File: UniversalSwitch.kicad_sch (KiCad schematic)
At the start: 30 parts, among them IC1501 TPS259830ONRGER, IC1502 TPS259830ONRGER, Q1501 NVTFWS4D9N04XMTAG, Q1502 NVTFWS4D9N04XMTAG

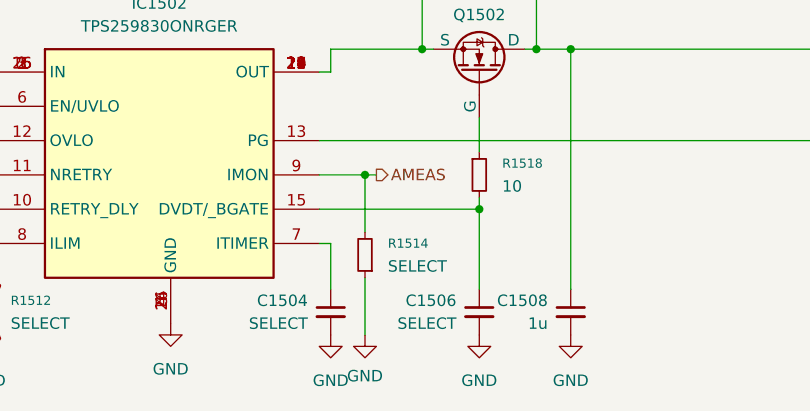
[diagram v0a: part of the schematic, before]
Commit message: Minor changes to acomodate jlcpcb guidelines, this version ordered
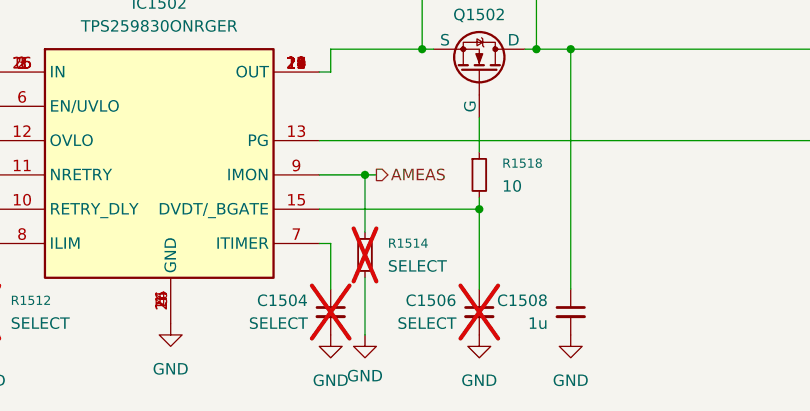
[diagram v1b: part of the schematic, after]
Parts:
- C1504, C1506, R1514: now not fitted

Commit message: nearly finnished CORE pcb
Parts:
- renumbered C1501 to C4502, C1502 to C4504, C1503 to C4506, C1504 to C4508, C1505 to C4509, C1506 to C4510, C1507 to C4511, C1508 to C4512, IC1501 to IC4501, IC1502 to IC4502, Q1501 to Q4501, Q1502 to Q4502, R1501 to R4502, R1502 to R4503, R1503 to R4504, R1504 to R4505, R1505 to R4506, R1506 to R4508, R1507 to R4509, R1508 to R4510, R1509 to R4511, R1510 to R4512, R1511 to R4513, R1512 to R4514, R1513 to R4515, R1514 to R4516, R1515 to R4517, R1516 to R4518, R1517 to R4519, R1518 to R4520

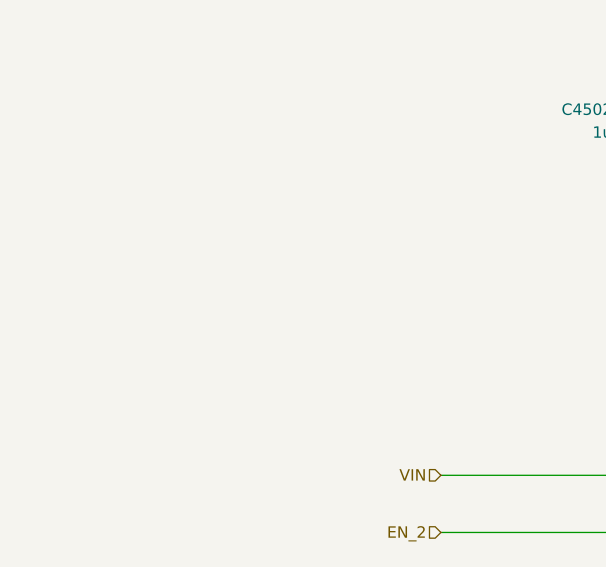
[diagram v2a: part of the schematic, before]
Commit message: pcb progres for all components
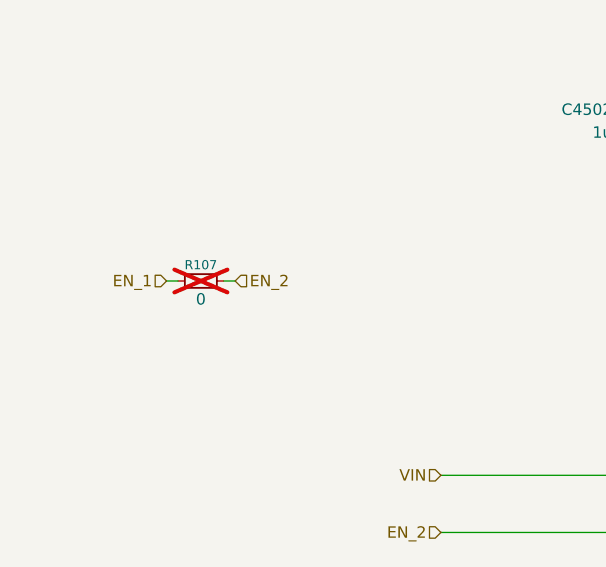
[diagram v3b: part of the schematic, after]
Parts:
- added R107: 0, Resistor_SMD:R_0603_1608Metric_Pad0.98x0.95mm_HandSolder, symbol Device:R_Small
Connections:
- net EN_1: now also R107.1
- net EN_2: now also R107.2

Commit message: progress on PCBs
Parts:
- removed R107: 0, Resistor_SMD:R_0603_1608Metric_Pad0.98x0.95mm_HandSolder, symbol Device:R_Small
- renumbered C4502 to C601, C4506 to C602, C4509 to C603, C4511 to C604, C4504 to C605, C4508 to C606, C4510 to C607, C4512 to C608, IC4501 to IC601, IC4502 to IC602, Q4501 to Q601, Q4502 to Q602, R4517 to R601, R4502 to R602, R4503 to R603, R4518 to R604, R4504 to R605, R4515 to R606, R4509 to R607, R4511 to R608, R4513 to R609, R4519 to R610, R4505 to R611, R4506 to R612, R4520 to R613, R4508 to R614, R4516 to R615, R4510 to R616, R4512 to R617, R4514 to R618
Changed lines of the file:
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@@
 	(wire
 		(pts
-			(xy 38.1 88.9) (xy 36.83 88.9)
-		)
-		(stroke
-			(width 0)
-			(type default)
-		)
-	)
-	(wire
-		(pts
 			(xy 182.88 118.11) (xy 182.88 121.92)
 		)
@@
 	(wire
 		(pts
-			(xy 44.45 88.9) (xy 43.18 88.9)
-		)
-		(stroke
-			(width 0)
-			(type default)
-		)
-	)
-	(wire
-		(pts
 			(xy 185.42 102.87) (xy 189.23 102.87)
 		)
@@
 		)
 	)
-	(hierarchical_label "EN_1"
-		(shape input)
-		(at 36.83 88.9 180)
-		(effects
-			(font
-				(size 1.27 1.27)
-			)
-			(justify right)
-		)
-	)
 	(hierarchical_label "EN_2"
 		(shape input)
@@
 		)
 	)
-	(hierarchical_label "EN_2"
-		(shape input)
-		(at 44.45 88.9 0)
-		(effects
-			(font
-				(size 1.27 1.27)
-			)
-			(justify left)
-		)
-	)
 	(symbol
 		(lib_id "Device:R_Small")
@@
 		(dnp yes)
 		(fields_autoplaced yes)
-		(property "Reference" "R4509"
+		(property "Reference" "R607"
 			(at 107.95 69.8499 0)
 			(effects
@@
 		(dnp no)
 		(fields_autoplaced yes)
-		(property "Reference" "R4502"
+		(property "Reference" "R602"
 			(at 96.52 44.4499 0)
 			(effects
@@
 		(dnp no)
 		(fields_autoplaced yes)
-		(property "Reference" "R4506"
+		(property "Reference" "R612"
 			(at 96.52 119.3799 0)
 			(effects
@@
 		(on_board yes)
 		(dnp yes)
-		(property "Reference" "C4510"
+		(property "Reference" "C607"
 			(at 180.34 138.4362 0)
 			(effects
@@
 		(on_board yes)
 		(dnp no)
-		(property "Reference" "C4511"
+		(property "Reference" "C604"
 			(at 190.5 69.8562 0)
 			(effects
@@
 		(on_board yes)
 		(dnp no)
-		(property "Reference" "#PWR04524"
+		(property "Reference" "#PWR0608"
 			(at 170.18 80.01 0)
 			(effects
@@
 		(on_board yes)
 		(dnp yes)
-		(property "Reference" "C4508"
+		(property "Reference" "C606"
 			(at 163.83 138.4362 0)
 			(effects
@@
 		(dnp no)
 		(fields_autoplaced yes)
-		(property "Reference" "IC4501"
+		(property "Reference" "IC601"
 			(at 147.32 36.83 0)
 			(effects
@@
 		(dnp no)
 		(fields_autoplaced yes)
-		(property "Reference" "R4515"
+		(property "Reference" "R606"
 			(at 172.72 63.4999 0)
 			(effects
@@
 		(dnp yes)
 		(fields_autoplaced yes)
-		(property "Reference" "R4513"
+		(property "Reference" "R609"
 			(at 130.81 69.8499 0)
 			(effects
@@
 		(dnp no)
 		(fields_autoplaced yes)
-		(property "Reference" "#PWR04516"
+		(property "Reference" "#PWR0606"
 			(at 128.27 80.01 0)
 			(effects
@@
 		(dnp yes)
 		(fields_autoplaced yes)
-		(property "Reference" "R4516"
+		(property "Reference" "R615"
 			(at 172.72 132.0799 0)
 			(effects
@@
 		(on_board yes)
 		(dnp no)
-		(property "Reference" "C4504"
+		(property "Reference" "C605"
 			(at 86.36 138.4362 0)
 			(effects
@@
 		(dnp yes)
 		(fields_autoplaced yes)
-		(property "Reference" "R4517"
+		(property "Reference" "R601"
 			(at 182.88 29.21 90)
 			(effects
@@
 		(dnp no)
 		(fields_autoplaced yes)
-		(property "Reference" "#PWR04528"
+		(property "Reference" "#PWR0610"
 			(at 193.04 80.01 0)
 			(effects
@@
 		(dnp no)
 		(fields_autoplaced yes)
-		(property "Reference" "#PWR04508"
+		(property "Reference" "#PWR0611"
 			(at 93.98 138.43 0)
 			(effects
@@
 		(on_board yes)
 		(dnp no)
-		(property "Reference" "C4506"
+		(property "Reference" "C602"
 			(at 163.83 69.8562 0)
 			(effects
@@
 		(dnp no)
 		(fields_autoplaced yes)
-		(property "Reference" "IC4502"
+		(property "Reference" "IC602"
 			(at 147.32 105.41 0)
 			(effects
@@
 		(dnp yes)
 		(fields_autoplaced yes)
-		(property "Reference" "R4511"
+		(property "Reference" "R608"
 			(at 119.38 69.8499 0)
 			(effects
@@
 		(dnp no)
 		(fields_autoplaced yes)
-		(property "Reference" "R4504"
+		(property "Reference" "R605"
 			(at 96.52 59.6899 0)
 			(effects
@@
 		(dnp no)
 		(fields_autoplaced yes)
-		(property "Reference" "#PWR04506"
+		(property "Reference" "#PWR0601"
 			(at 93.98 69.85 0)
 			(effects
@@
 		(dnp no)
 		(fields_autoplaced yes)
-		(property "Reference" "R4505"
+		(property "Reference" "R611"
 			(at 96.52 113.0299 0)
 			(effects
@@
 		(dnp no)
 		(fields_autoplaced yes)
-		(property "Reference" "R4518"
+		(property "Reference" "R604"
 			(at 185.42 54.6099 0)
 			(effects
@@
 	)
 	(symbol
-		(lib_id "Device:R_Small")
-		(at 40.64 88.9 90)
-		(unit 1)
-		(exclude_from_sim no)
-		(in_bom yes)
-		(on_board yes)
-		(dnp yes)
-		(property "Reference" "R107"
-			(at 40.64 87.122 90)
-			(effects
-				(font
-					(size 1.016 1.016)
-				)
-			)
-		)
-		(property "Value" "0"
-			(at 40.64 90.932 90)
-			(effects
-				(font
-					(size 1.27 1.27)
-				)
-			)
-		)
-		(property "Footprint" "Resistor_SMD:R_0603_1608Metric_Pad0.98x0.95mm_HandSolder"
-			(at 40.64 88.9 0)
-			(effects
-				(font
-					(size 1.27 1.27)
-				)
-				(hide yes)
-			)
-		)
-		(property "Datasheet" "~"
-			(at 40.64 88.9 0)
-			(effects
-				(font
-					(size 1.27 1.27)
-				)
-				(hide yes)
-			)
-		)
-		(property "Description" "Resistor, small symbol"
-			(at 40.64 88.9 0)
-			(effects
-				(font
-					(size 1.27 1.27)
-				)
-				(hide yes)
-			)
-		)
-		(pin "1"
-		)
-		(pin "2"
-		)
-		(instances
-			(project "EPS"
-				(path "/94201994-47b8-4213-8d1a-05da12b2a7b0/2939b268-15b7-411b-af55-ccc6daa126bc/de7fc528-e990-41c1-895c-f423d7320cf5"
-					(reference "R107")
-					(unit 1)
-				)
-			)
-		)
-	)
-	(symbol
 		(lib_id "power:GND")
 		(at 116.84 73.66 0)
@@
 		(dnp no)
 		(fields_autoplaced yes)
-		(property "Reference" "#PWR04512"
+		(property "Reference" "#PWR0605"
 			(at 116.84 80.01 0)
 			(effects
@@
 		(on_board yes)
 		(dnp no)
-		(property "Reference" "C4512"
+		(property "Reference" "C608"
 			(at 190.5 138.4362 0)
 			(effects
@@
 		(dnp no)
 		(fields_autoplaced yes)
-		(property "Reference" "#PWR04520"
+		(property "Reference" "#PWR0602"
 			(at 148.59 78.74 0)
 			(effects
@@
 		(dnp no)
 		(fields_autoplaced yes)
-		(property "Reference" "R4520"
+		(property "Reference" "R613"
 			(at 185.42 123.1899 0)
 			(effects
@@
 		(dnp no)
 		(fields_autoplaced yes)
-		(property "Reference" "#PWR04518"
+		(property "Reference" "#PWR0616"
 			(at 128.27 148.59 0)
 			(effects
@@
 		(dnp no)
 		(fields_autoplaced yes)
-		(property "Reference" "#PWR04526"
+		(property "Reference" "#PWR0609"
 			(at 182.88 80.01 0)
 			(effects
@@
 		(dnp no)
 		(fields_autoplaced yes)
-		(property "Reference" "#PWR04529"
+		(property "Reference" "#PWR0620"
 			(at 193.04 148.59 0)
 			(effects
@@
 		(dnp no)
 		(fields_autoplaced yes)
-		(property "Reference" "#PWR04523"
+		(property "Reference" "#PWR0617"
 			(at 166.37 148.59 0)
 			(effects
@@
 		(dnp no)
 		(fields_autoplaced yes)
-		(property "Reference" "#PWR04514"
+		(property "Reference" "#PWR0615"
 			(at 116.84 148.59 0)
 			(effects
@@
 		(dnp no)
 		(fields_autoplaced yes)
-		(property "Reference" "#PWR04511"
+		(property "Reference" "#PWR0614"
 			(at 105.41 148.59 0)
 			(effects
@@
 		(dnp no)
 		(fields_autoplaced yes)
-		(property "Reference" "R4503"
+		(property "Reference" "R603"
 			(at 96.52 50.7999 0)
 			(effects
@@
 		(dnp yes)
 		(fields_autoplaced yes)
-		(property "Reference" "R4514"
+		(property "Reference" "R618"
 			(at 130.81 138.4299 0)
 			(effects
@@
 		(dnp no)
 		(fields_autoplaced yes)
-		(property "Reference" "#PWR04510"
+		(property "Reference" "#PWR0604"
 			(at 105.41 80.01 0)
 			(effects
@@
 		(dnp no)
 		(fields_autoplaced yes)
-		(property "Reference" "#PWR04527"
+		(property "Reference" "#PWR0619"
 			(at 182.88 148.59 0)
 			(effects
@@
 		(dnp no)
 		(fields_autoplaced yes)
-		(property "Reference" "R4508"
+		(property "Reference" "R614"
 			(at 96.52 128.2699 0)
 			(effects
@@
 		(on_board yes)
 		(dnp no)
-		(property "Reference" "Q4501"
+		(property "Reference" "Q601"
 			(at 182.88 38.1 90)
 			(effects
@@
 		(on_board yes)
 		(dnp no)
-		(property "Reference" "C4502"
+		(property "Reference" "C601"
 			(at 86.36 69.8562 0)
 			(effects
@@
 		(dnp yes)
 		(fields_autoplaced yes)
-		(property "Reference" "R4512"
+		(property "Reference" "R617"
 			(at 119.38 138.4299 0)
 			(effects
@@
 		(on_board yes)
 		(dnp no)
-		(property "Reference" "Q4502"
+		(property "Reference" "Q602"
 			(at 182.88 106.68 90)
 			(effects
@@
 		(on_board yes)
 		(dnp no)
-		(property "Reference" "C4509"
+		(property "Reference" "C603"
 			(at 180.34 69.8562 0)
 			(effects
@@
 		(dnp no)
 		(fields_autoplaced yes)
-		(property "Reference" "#PWR04522"
+		(property "Reference" "#PWR0607"
 			(at 166.37 80.01 0)
 			(effects
@@
 		(dnp no)
 		(fields_autoplaced yes)
-		(property "Reference" "#PWR04504"
+		(property "Reference" "#PWR0613"
 			(at 88.9 148.59 0)
 			(effects
@@
 		(dnp yes)
 		(fields_autoplaced yes)
-		(property "Reference" "R4510"
+		(property "Reference" "R616"
 			(at 107.95 138.4299 0)
 			(effects
@@
 		(dnp no)
 		(fields_autoplaced yes)
-		(property "Reference" "#PWR04521"
+		(property "Reference" "#PWR0612"
 			(at 148.59 147.32 0)
 			(effects
@@
 		(on_board yes)
 		(dnp no)
-		(property "Reference" "#PWR04525"
+		(property "Reference" "#PWR0618"
 			(at 170.18 148.59 0)
 			(effects
@@
 		(dnp yes)
 		(fields_autoplaced yes)
-		(property "Reference" "R4519"
+		(property "Reference" "R610"
 			(at 182.88 97.79 90)
 			(effects
@@
 		(dnp no)
 		(fields_autoplaced yes)
-		(property "Reference" "#PWR04502"
+		(property "Reference" "#PWR0603"
 			(at 88.9 80.01 0)
 			(effects
